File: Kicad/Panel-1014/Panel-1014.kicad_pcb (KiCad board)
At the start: 2 copper layers, 88.9 x 81.3 mm, 192 parts, among them P1 TST, P2 CONN_4, P3 CONN_4, P4 SPADE_187, P5 CONN_8, P6 CONN_2, P7 CONN_8, Q1 MOSFET_N, Q2 MOSFET_N, Q3 MOSFET_N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

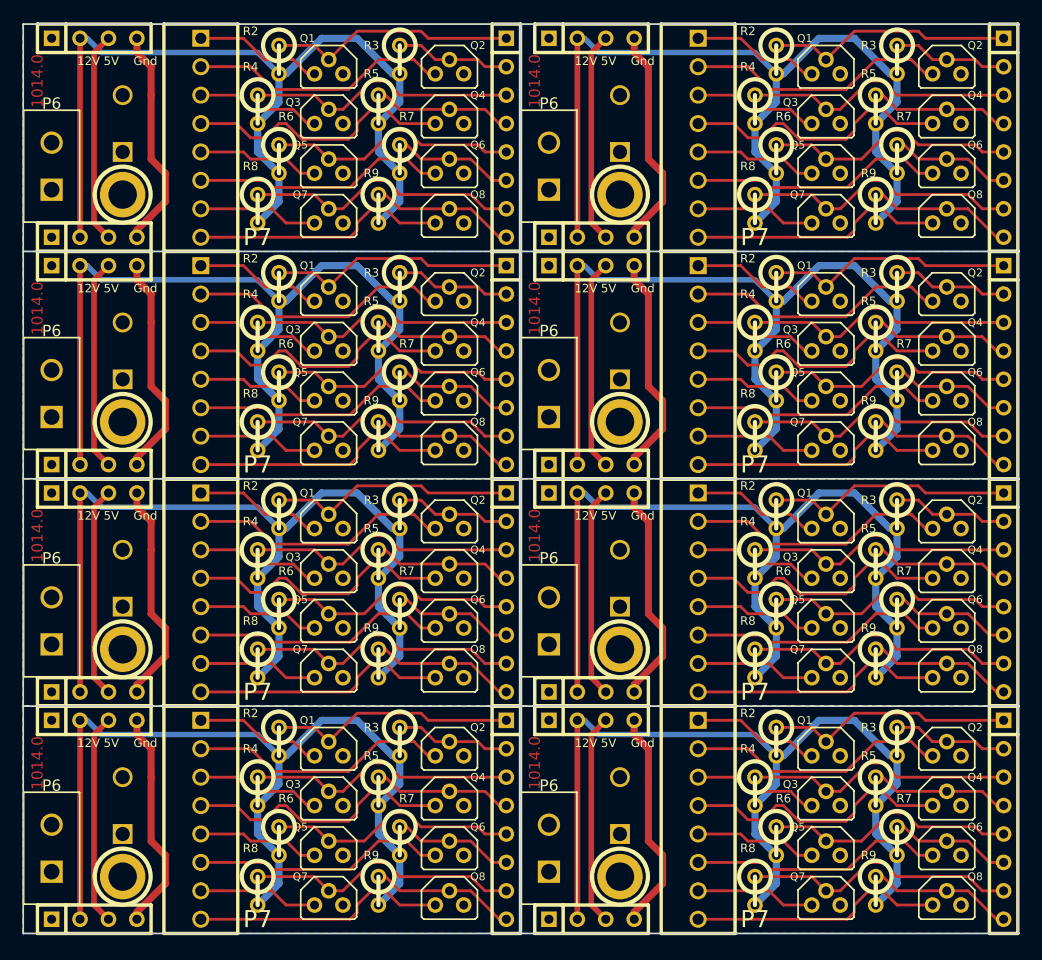
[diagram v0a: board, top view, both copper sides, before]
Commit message: Kicad updates: Added IncandWing (1014.zip), PwrFilter (1018.zip), updated Sol Panel (Panel-1013.zip), Incand Panel (Panel-1014.zip), and Pwr Filter Panel (Panel-1018.zip).  Panels had a different drill origin than PCB origin.
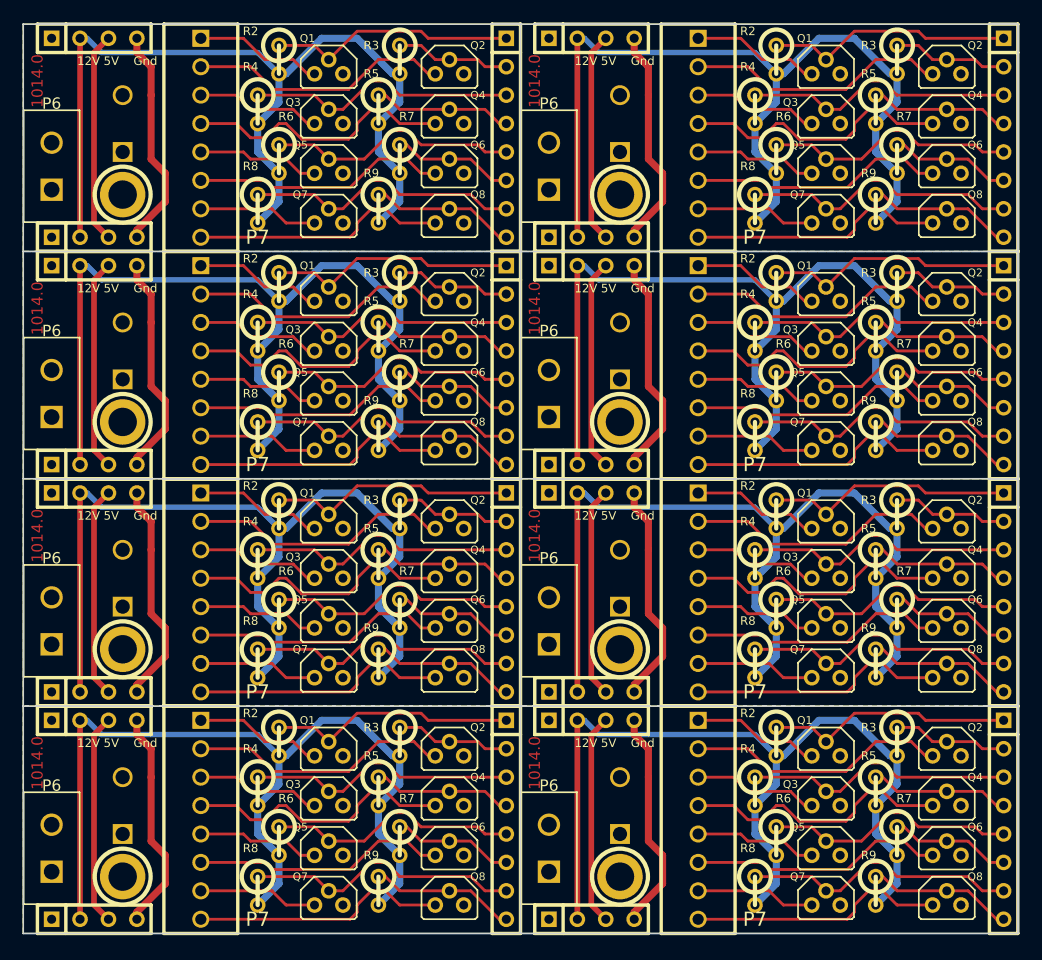
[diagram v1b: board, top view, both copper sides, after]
